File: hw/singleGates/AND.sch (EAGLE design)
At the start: 8 parts, among them Q1 BC817, Q2 BC817, Q3 BC817

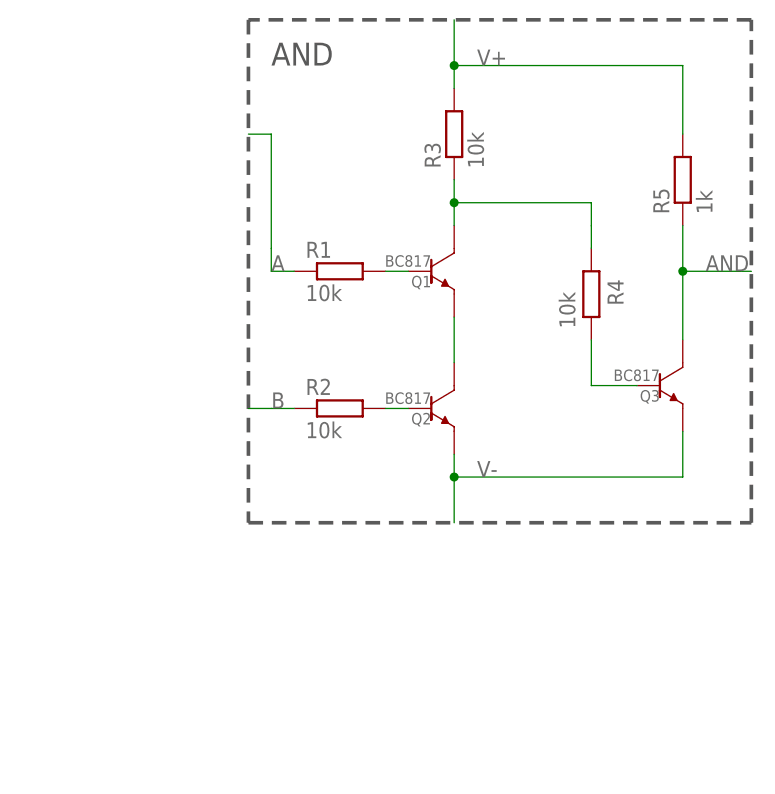
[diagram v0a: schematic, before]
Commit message: Updated gates to be centered
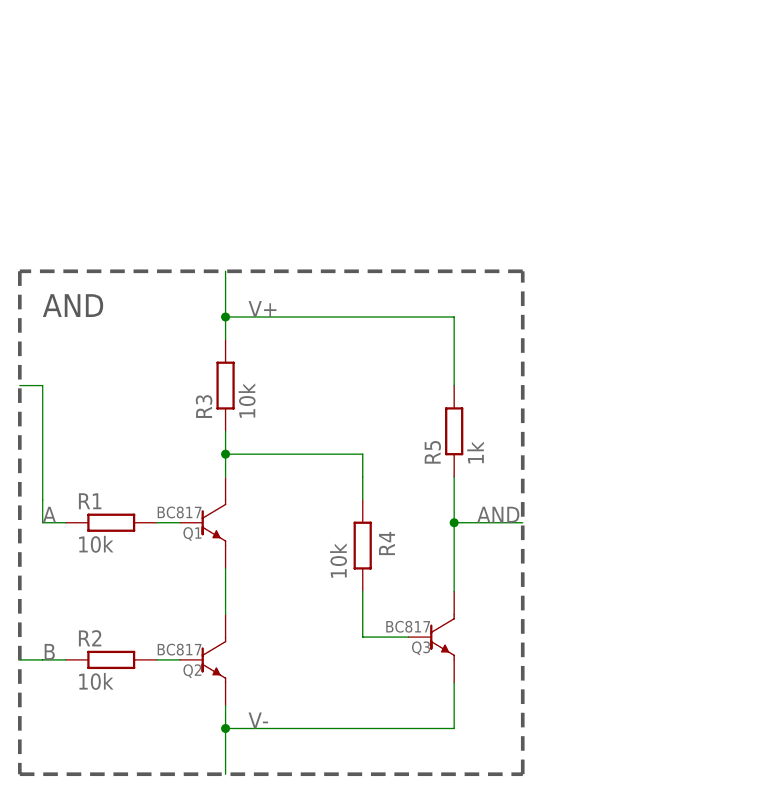
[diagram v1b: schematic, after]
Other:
- moved on the sheet: Q1, Q2, Q3, R1, R2, R3, R4, R5
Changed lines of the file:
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@@
 <sheet>
 <plain>
-<wire x1="55.88" y1="0" x2="55.88" y2="55.88" width="0.4064" layer="97" style="longdash"/>
-<wire x1="55.88" y1="55.88" x2="0" y2="55.88" width="0.4064" layer="97" style="longdash"/>
-<wire x1="0" y1="55.88" x2="0" y2="0" width="0.4064" layer="97" style="longdash"/>
-<wire x1="0" y1="0" x2="55.88" y2="0" width="0.4064" layer="97" style="longdash"/>
-<text x="2.54" y="50.8" size="2.54" layer="97" ratio="12">AND</text>
+<wire x1="30.48" y1="-27.94" x2="30.48" y2="27.94" width="0.4064" layer="97" style="longdash"/>
+<wire x1="30.48" y1="27.94" x2="-25.4" y2="27.94" width="0.4064" layer="97" style="longdash"/>
+<wire x1="-25.4" y1="27.94" x2="-25.4" y2="-27.94" width="0.4064" layer="97" style="longdash"/>
+<wire x1="-25.4" y1="-27.94" x2="30.48" y2="-27.94" width="0.4064" layer="97" style="longdash"/>
+<text x="-22.86" y="22.86" size="2.54" layer="97" ratio="12">AND</text>
 </plain>
 <instances>
-<instance part="R1" gate="G$1" x="10.16" y="27.94"/>
-<instance part="R2" gate="G$1" x="10.16" y="12.7"/>
-<instance part="R3" gate="G$1" x="22.86" y="43.18" rot="R90"/>
-<instance part="R4" gate="G$1" x="38.1" y="25.4" smashed="yes" rot="R90">
-<attribute name="NAME" x="41.6814" y="24.13" size="1.778" layer="95" rot="R90"/>
-<attribute name="VALUE" x="36.322" y="21.59" size="1.778" layer="96" rot="R90"/>
+<instance part="R1" gate="G$1" x="-15.24" y="0"/>
+<instance part="R2" gate="G$1" x="-15.24" y="-15.24"/>
+<instance part="R3" gate="G$1" x="-2.54" y="15.24" rot="R90"/>
+<instance part="R4" gate="G$1" x="12.7" y="-2.54" smashed="yes" rot="R90">
+<attribute name="NAME" x="16.2814" y="-3.81" size="1.778" layer="95" rot="R90"/>
+<attribute name="VALUE" x="10.922" y="-6.35" size="1.778" layer="96" rot="R90"/>
 </instance>
-<instance part="R5" gate="G$1" x="48.26" y="38.1" rot="R90"/>
-<instance part="Q1" gate="G$1" x="22.86" y="27.94" smashed="yes">
-<attribute name="NAME" x="20.32" y="26.162" size="1.27" layer="95" ratio="12" rot="R180" align="top-left"/>
-<attribute name="VALUE" x="20.32" y="29.718" size="1.27" layer="96" ratio="12" rot="R180"/>
+<instance part="R5" gate="G$1" x="22.86" y="10.16" rot="R90"/>
+<instance part="Q1" gate="G$1" x="-2.54" y="0" smashed="yes">
+<attribute name="NAME" x="-5.08" y="-1.778" size="1.27" layer="95" ratio="12" rot="R180" align="top-left"/>
+<attribute name="VALUE" x="-5.08" y="1.778" size="1.27" layer="96" ratio="12" rot="R180"/>
 </instance>
-<instance part="Q2" gate="G$1" x="22.86" y="12.7" smashed="yes">
-<attribute name="NAME" x="20.32" y="10.922" size="1.27" layer="95" ratio="12" rot="R180" align="top-left"/>
-<attribute name="VALUE" x="20.32" y="14.478" size="1.27" layer="96" ratio="12" rot="R180"/>
+<instance part="Q2" gate="G$1" x="-2.54" y="-15.24" smashed="yes">
+<attribute name="NAME" x="-5.08" y="-17.018" size="1.27" layer="95" ratio="12" rot="R180" align="top-left"/>
+<attribute name="VALUE" x="-5.08" y="-13.462" size="1.27" layer="96" ratio="12" rot="R180"/>
 </instance>
-<instance part="Q3" gate="G$1" x="48.26" y="15.24" smashed="yes">
-<attribute name="NAME" x="45.72" y="13.462" size="1.27" layer="95" ratio="12" rot="R180" align="top-left"/>
-<attribute name="VALUE" x="45.72" y="17.018" size="1.27" layer="96" ratio="12" rot="R180"/>
+<instance part="Q3" gate="G$1" x="22.86" y="-12.7" smashed="yes">
+<attribute name="NAME" x="20.32" y="-14.478" size="1.27" layer="95" ratio="12" rot="R180" align="top-left"/>
+<attribute name="VALUE" x="20.32" y="-10.922" size="1.27" layer="96" ratio="12" rot="R180"/>
 </instance>
 </instances>
@@
 <pinref part="R1" gate="G$1" pin="2"/>
 <pinref part="Q1" gate="G$1" pin="BASE"/>
-<wire x1="15.24" y1="27.94" x2="17.78" y2="27.94" width="0.1524" layer="91"/>
+<wire x1="-10.16" y1="0" x2="-7.62" y2="0" width="0.1524" layer="91"/>
 </segment>
 </net>
@@
 <pinref part="R2" gate="G$1" pin="2"/>
 <pinref part="Q2" gate="G$1" pin="BASE"/>
-<wire x1="15.24" y1="12.7" x2="17.78" y2="12.7" width="0.1524" layer="91"/>
+<wire x1="-10.16" y1="-15.24" x2="-7.62" y2="-15.24" width="0.1524" layer="91"/>
 </segment>
 </net>
@@
 <segment>
 <pinref part="R4" gate="G$1" pin="1"/>
-<wire x1="38.1" y1="15.24" x2="38.1" y2="20.32" width="0.1524" layer="91"/>
+<wire x1="12.7" y1="-12.7" x2="12.7" y2="-7.62" width="0.1524" layer="91"/>
 <pinref part="Q3" gate="G$1" pin="BASE"/>
-<wire x1="43.18" y1="15.24" x2="38.1" y2="15.24" width="0.1524" layer="91"/>
+<wire x1="17.78" y1="-12.7" x2="12.7" y2="-12.7" width="0.1524" layer="91"/>
 </segment>
 </net>
@@
 <segment>
 <pinref part="R3" gate="G$1" pin="1"/>
-<wire x1="22.86" y1="38.1" x2="22.86" y2="35.56" width="0.1524" layer="91"/>
-<wire x1="38.1" y1="33.02" x2="38.1" y2="35.56" width="0.1524" layer="91"/>
-<wire x1="38.1" y1="35.56" x2="22.86" y2="35.56" width="0.1524" layer="91"/>
-<junction x="22.86" y="35.56"/>
+<wire x1="-2.54" y1="10.16" x2="-2.54" y2="7.62" width="0.1524" layer="91"/>
+<wire x1="12.7" y1="5.08" x2="12.7" y2="7.62" width="0.1524" layer="91"/>
+<wire x1="12.7" y1="7.62" x2="-2.54" y2="7.62" width="0.1524" layer="91"/>
+<junction x="-2.54" y="7.62"/>
 <pinref part="R4" gate="G$1" pin="2"/>
-<wire x1="38.1" y1="30.48" x2="38.1" y2="33.02" width="0.1524" layer="91"/>
+<wire x1="12.7" y1="2.54" x2="12.7" y2="5.08" width="0.1524" layer="91"/>
 <pinref part="Q1" gate="G$1" pin="COLLECTOR"/>
-<wire x1="22.86" y1="35.56" x2="22.86" y2="33.02" width="0.1524" layer="91"/>
+<wire x1="-2.54" y1="7.62" x2="-2.54" y2="5.08" width="0.1524" layer="91"/>
 </segment>
 </net>
@@
 <segment>
 <pinref part="R1" gate="G$1" pin="1"/>
-<wire x1="5.08" y1="27.94" x2="2.54" y2="27.94" width="0.1524" layer="91"/>
-<wire x1="2.54" y1="27.94" x2="2.54" y2="30.48" width="0.1524" layer="91"/>
-<wire x1="2.54" y1="30.48" x2="2.54" y2="43.18" width="0.1524" layer="91"/>
-<wire x1="2.54" y1="43.18" x2="0" y2="43.18" width="0.1524" layer="91"/>
-<label x="2.54" y="27.94" size="1.778" layer="95"/>
+<wire x1="-20.32" y1="0" x2="-22.86" y2="0" width="0.1524" layer="91"/>
+<wire x1="-22.86" y1="0" x2="-22.86" y2="2.54" width="0.1524" layer="91"/>
+<wire x1="-22.86" y1="2.54" x2="-22.86" y2="15.24" width="0.1524" layer="91"/>
+<wire x1="-22.86" y1="15.24" x2="-25.4" y2="15.24" width="0.1524" layer="91"/>
+<label x="-22.86" y="0" size="1.778" layer="95"/>
 </segment>
 </net>
@@
 <segment>
 <pinref part="R2" gate="G$1" pin="1"/>
-<wire x1="5.08" y1="12.7" x2="2.54" y2="12.7" width="0.1524" layer="91"/>
-<wire x1="2.54" y1="12.7" x2="0" y2="12.7" width="0.1524" layer="91"/>
-<label x="2.54" y="12.7" size="1.778" layer="95"/>
+<wire x1="-20.32" y1="-15.24" x2="-22.86" y2="-15.24" width="0.1524" layer="91"/>
+<wire x1="-22.86" y1="-15.24" x2="-25.4" y2="-15.24" width="0.1524" layer="91"/>
+<label x="-22.86" y="-15.24" size="1.778" layer="95"/>
 </segment>
 </net>
@@
 <segment>
 <pinref part="R5" gate="G$1" pin="1"/>
-<wire x1="48.26" y1="27.94" x2="48.26" y2="33.02" width="0.1524" layer="91"/>
-<wire x1="48.26" y1="27.94" x2="55.88" y2="27.94" width="0.1524" layer="91"/>
-<junction x="48.26" y="27.94"/>
-<label x="50.8" y="27.94" size="1.778" layer="95"/>
+<wire x1="22.86" y1="0" x2="22.86" y2="5.08" width="0.1524" layer="91"/>
+<wire x1="22.86" y1="0" x2="30.48" y2="0" width="0.1524" layer="91"/>
+<junction x="22.86" y="0"/>
+<label x="25.4" y="0" size="1.778" layer="95"/>
 <pinref part="Q3" gate="G$1" pin="COLLECTOR"/>
-<wire x1="48.26" y1="27.94" x2="48.26" y2="20.32" width="0.1524" layer="91"/>
+<wire x1="22.86" y1="0" x2="22.86" y2="-7.62" width="0.1524" layer="91"/>
 </segment>
 </net>
@@
 <pinref part="R3" gate="G$1" pin="2"/>
 <pinref part="R5" gate="G$1" pin="2"/>
-<wire x1="22.86" y1="50.8" x2="22.86" y2="48.26" width="0.1524" layer="91"/>
-<wire x1="48.26" y1="50.8" x2="48.26" y2="43.18" width="0.1524" layer="91"/>
-<wire x1="22.86" y1="50.8" x2="48.26" y2="50.8" width="0.1524" layer="91"/>
-<wire x1="22.86" y1="50.8" x2="22.86" y2="55.88" width="0.1524" layer="91"/>
-<label x="25.4" y="50.8" size="1.778" layer="95"/>
-<junction x="22.86" y="50.8"/>
+<wire x1="-2.54" y1="22.86" x2="-2.54" y2="20.32" width="0.1524" layer="91"/>
+<wire x1="22.86" y1="22.86" x2="22.86" y2="15.24" width="0.1524" layer="91"/>
+<wire x1="-2.54" y1="22.86" x2="22.86" y2="22.86" width="0.1524" layer="91"/>
+<wire x1="-2.54" y1="22.86" x2="-2.54" y2="27.94" width="0.1524" layer="91"/>
+<label x="0" y="22.86" size="1.778" layer="95"/>
+<junction x="-2.54" y="22.86"/>
 </segment>
 </net>
 <net name="V-" class="0">
 <segment>
-<wire x1="22.86" y1="5.08" x2="48.26" y2="5.08" width="0.1524" layer="91"/>
-<wire x1="22.86" y1="5.08" x2="22.86" y2="0" width="0.1524" layer="91"/>
-<label x="25.4" y="5.08" size="1.778" layer="95"/>
-<junction x="22.86" y="5.08"/>
+<wire x1="-2.54" y1="-22.86" x2="22.86" y2="-22.86" width="0.1524" layer="91"/>
+<wire x1="-2.54" y1="-22.86" x2="-2.54" y2="-27.94" width="0.1524" layer="91"/>
+<label x="0" y="-22.86" size="1.778" layer="95"/>
+<junction x="-2.54" y="-22.86"/>
 <pinref part="Q2" gate="G$1" pin="EMITTER"/>
 <pinref part="Q3" gate="G$1" pin="EMITTER"/>
-<wire x1="22.86" y1="7.62" x2="22.86" y2="5.08" width="0.1524" layer="91"/>
-<wire x1="48.26" y1="10.16" x2="48.26" y2="5.08" width="0.1524" layer="91"/>
+<wire x1="-2.54" y1="-20.32" x2="-2.54" y2="-22.86" width="0.1524" layer="91"/>
+<wire x1="22.86" y1="-17.78" x2="22.86" y2="-22.86" width="0.1524" layer="91"/>
 </segment>
 </net>
@@
 <pinref part="Q2" gate="G$1" pin="COLLECTOR"/>
 <pinref part="Q1" gate="G$1" pin="EMITTER"/>
-<wire x1="22.86" y1="22.86" x2="22.86" y2="17.78" width="0.1524" layer="91"/>
+<wire x1="-2.54" y1="-5.08" x2="-2.54" y2="-10.16" width="0.1524" layer="91"/>
 </segment>
 </net>

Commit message: First full test suite
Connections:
- net V+ renamed _VP
- net V- renamed _VN
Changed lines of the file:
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@@
 <?xml version="1.0" encoding="utf-8"?>
 <!DOCTYPE eagle SYSTEM "eagle.dtd">
-<eagle version="7.4.0">
+<eagle version="7.3.0">
 <drawing>
 <settings>
@@
 </segment>
 </net>
-<net name="V+" class="0">
+<net name="_VP" class="0">
 <segment>
 <pinref part="R3" gate="G$1" pin="2"/>
@@
 </segment>
 </net>
-<net name="V-" class="0">
+<net name="_VN" class="0">
 <segment>
 <wire x1="-2.54" y1="-22.86" x2="22.86" y2="-22.86" width="0.1524" layer="91"/>
